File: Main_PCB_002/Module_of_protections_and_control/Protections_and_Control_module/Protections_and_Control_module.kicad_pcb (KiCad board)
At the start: 2 copper layers, 55 x 15 mm, 66 parts, among them Q1 AON7407, Q2 AON7407, Q3 BSS123, Q4 BSS123, Q5 AON7407, Q6 AON7407, U1 TL331, U2 ATtiny25-20S, U2 Mounting_Hole_M2, U3 Mounting_Hole_M2, U4 Mounting_Hole_M2, U5 Mounting_Hole_M2

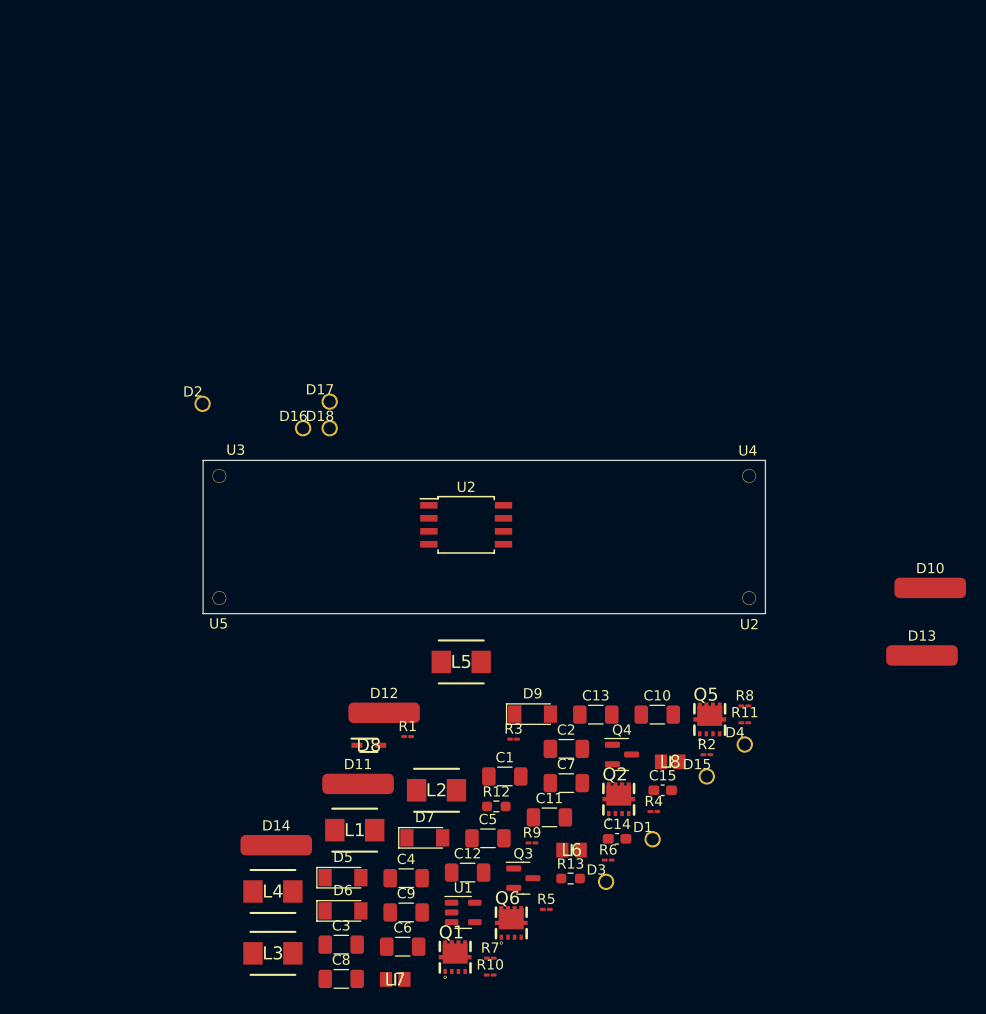
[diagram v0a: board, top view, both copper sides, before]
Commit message: Module of protections and control
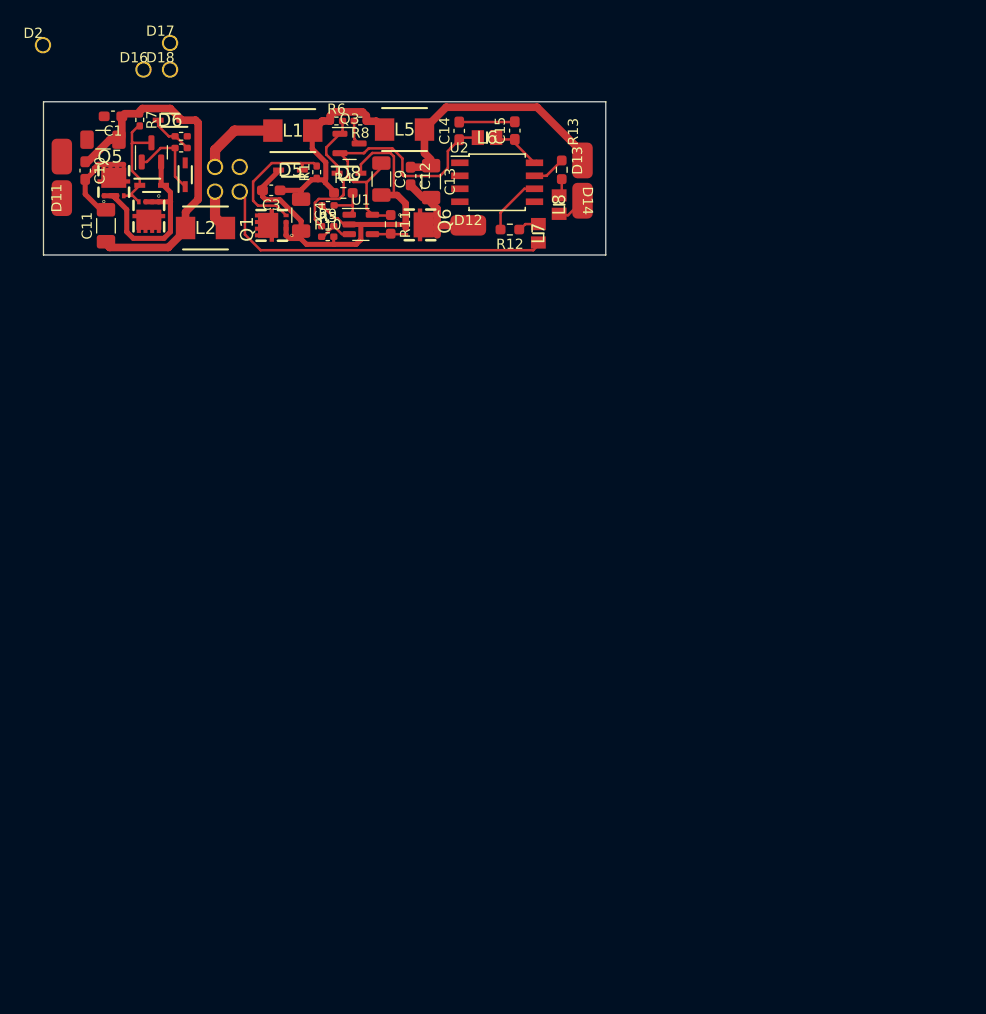
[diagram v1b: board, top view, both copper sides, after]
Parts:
- removed C5, C6, C7, C8: C, Capacitor_SMD:C_1206_3216Metric_Pad1.33x1.80mm_HandSolder
- removed L3, L4: TFM201610ALC-R47MTAA, libraries:INDPM4442X200N
- removed the U2 at (167.4, 74.5)
- removed U3, U4, U5: Mounting_Hole_M2, mount_holes:Hole_screw_M1p2
- C1, C10, C12, C3: footprint Capacitor_SMD:C_1206_3216Metric_Pad1.33x1.80mm_HandSolder -> Capacitor_SMD:C_0603_1608Metric_Pad1.08x0.95mm_HandSolder
- D10, D11, D12, D13, D14: footprint Flat_Wires_Pads:Flat_Wire_Pad_7X2mm -> Flat_Wires_Pads:Flat_Wire_Pad_3.5X2mm
- D5, D6, D7, D9: footprint Diode_SMD:D_MiniMELF -> libraries:SOD2513X120N
- R1, R10, R2, R3, R5, R6, R7, R8, R9: footprint Resistor_SMD:R_01005_0402Metric_Pad0.57x0.30mm_HandSolder -> Resistor_SMD:R_0402_1005Metric_Pad0.72x0.64mm_HandSolder
- R11, R4: footprint Resistor_SMD:R_01005_0402Metric_Pad0.57x0.30mm_HandSolder -> Resistor_SMD:R_0603_1608Metric_Pad0.98x0.95mm_HandSolder
- moved D10 94.8 mm to (100.2, 31.4), turned to 90 degrees
- moved R7 88.9 mm to (107.8, 27.8), turned to -90 degrees
- moved D3 79.7 mm to (115.2, 32.4), turned to 90 degrees
- moved R2 79.4 mm to (111.9, 29.4)
- moved D6 79.2 mm to (110.8, 27.8), turned to 180 degrees
- moved Q5 78.5 mm to (105.3, 33.8)
- moved C10 77.2 mm to (102.5, 32.7), turned to -90 degrees
- moved R6 77.0 mm to (127.1, 27.9)
- moved D1 76.4 mm to (115.2, 34.8), turned to 90 degrees
- moved C1 75.1 mm to (105.2, 27.4), turned to 180 degrees
- moved D4 75.0 mm to (117.6, 32.4), turned to 90 degrees
- moved C2 74.9 mm to (104.2, 29.7), turned to 180 degrees
- moved Q4 74.7 mm to (109.0, 31.0), turned to 90 degrees
- moved L7 74.3 mm to (146.8, 38.9), turned to -90 degrees
- moved C3 74.1 mm to (120.7, 34.7), turned to 180 degrees
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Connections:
- C10 pad 1: Net-(C10-Pad1) -> Net-(C1-Pad1)
- C11 pad 1: Net-(C10-Pad1) -> Net-(C1-Pad1)
- D10 pad 1: Net-(C10-Pad1) -> Net-(C1-Pad1)
- L5 pad 1: Net-(C5-Pad1) -> Net-(C3-Pad1)
- Q5 pad 10: (no net) -> Net-(C10-Pad2)
- Q5 pad 11: (no net) -> Net-(C10-Pad2)
- Q5 pad 9: (no net) -> Net-(C10-Pad2)
- Q6 pad 10: (no net) -> Net-(C12-Pad2)
- Q6 pad 11: (no net) -> Net-(C12-Pad2)
- Q6 pad 9: (no net) -> Net-(C12-Pad2)
- R4 pad 1: Net-(C5-Pad1) -> Net-(C3-Pad1)
- R6 pad 1: Net-(C5-Pad1) -> Net-(C3-Pad1)
- R8 pad 1: Net-(C5-Pad1) -> Net-(C3-Pad1)
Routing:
- net Net-(C3-Pad1): track 0.00 -> 61.1 mm
- net Net-(C3-Pad2): track 0.00 -> 46.0 mm
- net Net-(C1-Pad1): track 0.00 -> 35.0 mm
- net Net-(D15-Pad1): track 8.51 -> 42.7 mm
- net Net-(C12-Pad1): track 0.00 -> 24.9 mm
- net Net-(D9-Pad2): track 0.00 -> 20.5 mm
- net Net-(D5-Pad1): track 0.00 -> 13.7 mm
- net Net-(D9-Pad1): track 0.00 -> 11.6 mm
- net Net-(C12-Pad2): track 0.00 -> 9.70 mm
- net Net-(C10-Pad2): track 0.00 -> 8.64 mm
- net Net-(D3-Pad1): track 0.00 -> 8.10 mm
- net Net-(D7-Pad1): track 0.00 -> 8.02 mm
- net Net-(D8-Pad1): track 0.00 -> 6.11 mm
- net Net-(R12-Pad2): track 0.00 -> 5.94 mm
- net GND: track 0.00 -> 5.45 mm
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
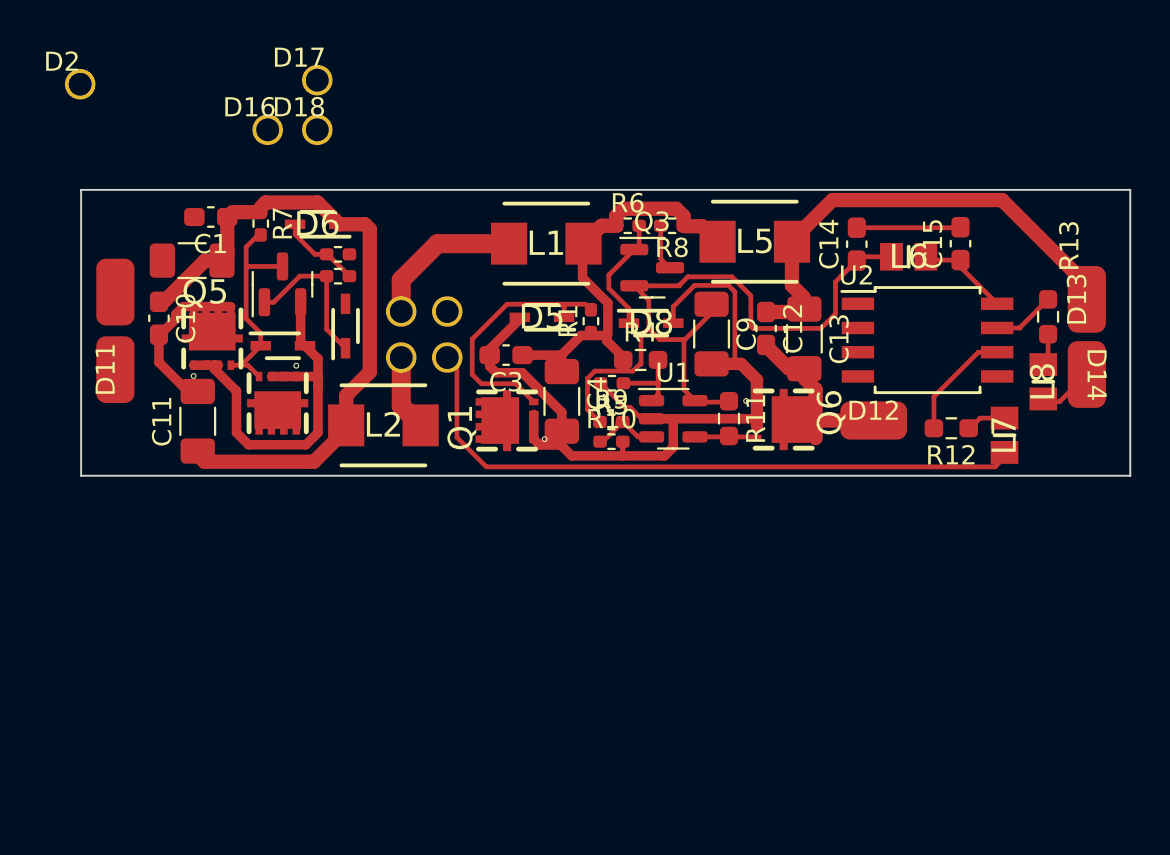
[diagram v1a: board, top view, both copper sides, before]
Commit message: Module of protections and control
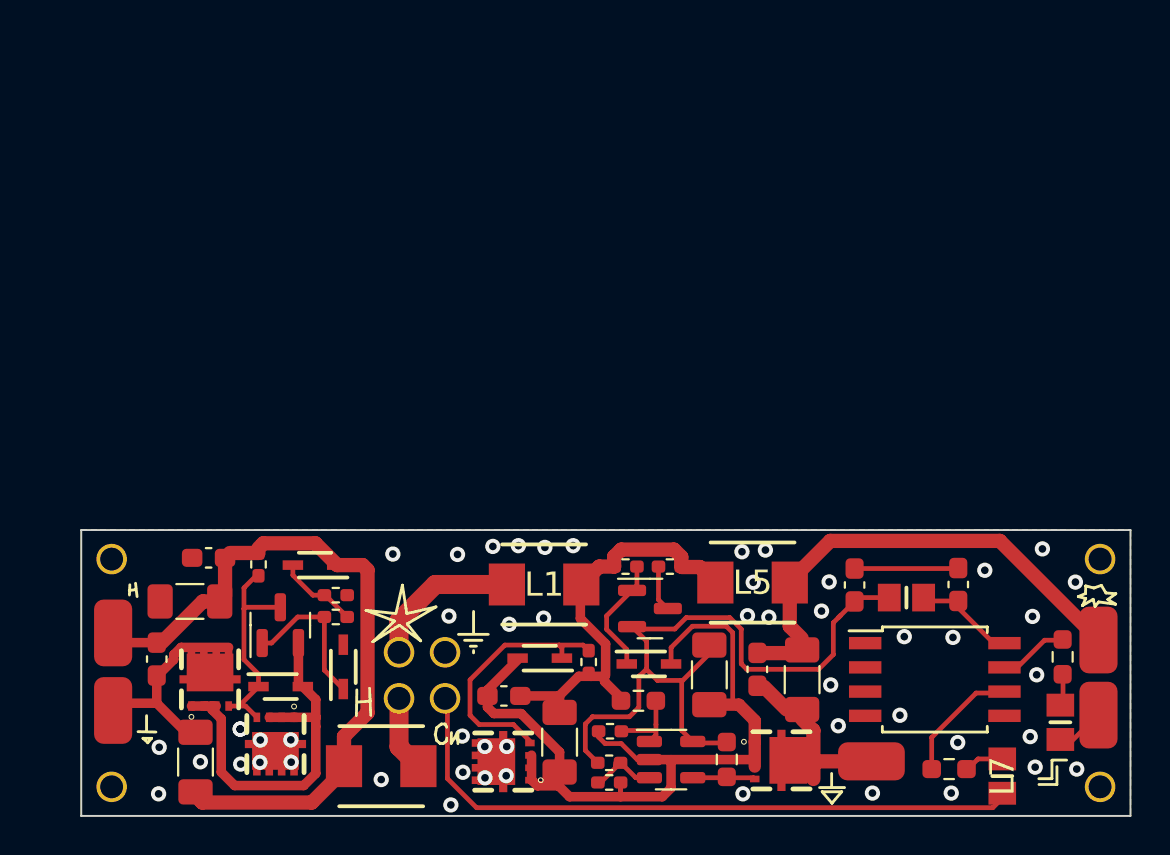
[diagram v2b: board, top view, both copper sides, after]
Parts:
- moved D16 55.6 mm to (151.8, 57.3)
- moved D18 46.8 mm to (151.8, 45.4)
- moved D2 36.9 mm to (100.0, 57.3)
- moved D17 27.3 mm to (100.0, 45.4)
- moved R5 18.2 mm to (126.1, 54.4)
- moved Q1 17.9 mm to (120.5, 56.0)
- moved C12 17.9 mm to (133.9, 51.1)
- moved L8 17.9 mm to (149.7, 53.9)
- moved C1 17.9 mm to (105.1, 45.3)
- moved C2 17.9 mm to (104.1, 47.6)
- moved D6 17.9 mm to (110.7, 45.7)
- moved L5 17.9 mm to (133.6, 46.6)
- moved L6 17.9 mm to (141.7, 47.4)
- moved R6 17.9 mm to (126.9, 45.8)
- moved R8 17.9 mm to (129.3, 45.8)
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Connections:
- Q1 pad 10: (no net) -> GND
- Q1 pad 11: (no net) -> GND
- Q1 pad 9: (no net) -> GND
- Q2 pad 10: (no net) -> GND
- Q2 pad 11: (no net) -> GND
- Q2 pad 9: (no net) -> GND
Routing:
- net GND: track 5.45 -> 92.0 mm, vias 0 -> 51
- net Net-(C14-Pad1): track 10.3 -> 58.9 mm
- net Net-(C3-Pad1): track 61.1 -> 22.9 mm
- net Net-(D15-Pad1): track 42.7 -> 51.5 mm
- net Net-(C1-Pad1): track 35.0 -> 37.5 mm
- net Net-(C10-Pad2): track 8.64 -> 11.1 mm
- net Net-(R13-Pad1): track 3.30 -> 3.96 mm
- added copper zone on B.Cu, net GND
- added copper zone on F.Cu, net GND
